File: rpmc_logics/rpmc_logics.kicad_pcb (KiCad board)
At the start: 2 copper layers, 56 x 60.5 mm, 9 parts, among them J1 Raspberry_Pi_2_3, J2 Conn_02x20_Odd_Even, U1 74HC373, U2 74HC373, U3 74LS139, U4 74LS139, U5 74LS139, U6 74HC04, U7 TXB0108PWR

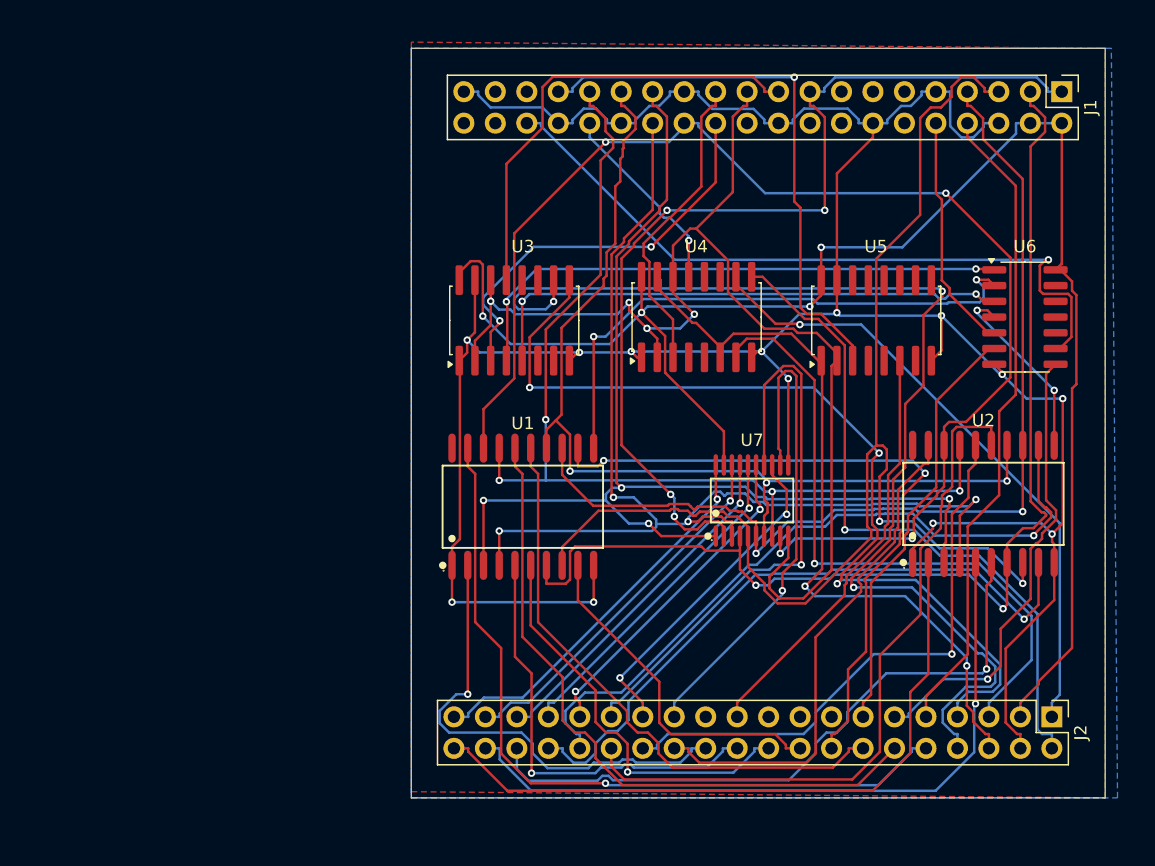
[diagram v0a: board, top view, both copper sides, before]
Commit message: libraries/PCM1808_EVB.kicad_mod libraries/footprint/PCM1808_EVB.kicad_mod libraries/footprint/msx-cartridge/libraries/packages3d/SOIC-20_L13.0-W7.6-P1.27-LS10.3-BL.step libraries/msx.pretty/Library.pretty/PCM1808_EVB.kicad_mod libraries/msx.pretty/PCM1808_EVB.kicad_mod libraries/msx_slot.kicad_sym libraries/footprint/msx-cartridge/libraries/packages3d/TSSOP-20_L6.5-W4.4-P0.65-LS6.4-BL.step -> libraries/packages3d/TSSOP-20_L6.5-W4.4-P0.65-LS6.4-BL.step rpmc_epm240/fp-info-cache rpmc_epm240/fp-lib-table rpmc_epm240/rpmc_epm240-backups/rpmc_epm240-2024-09-23_004329.zip rpmc_epm240/rpmc_epm240-backups/rpmc_epm240-2024-09-23_005415.zip rpmc_epm240/rpmc_epm240-backups/rpmc_epm240-2024-09-23_010603.zip rpmc_epm240/rpmc_epm240-backups/rpmc_epm240-2024-09-23_011813.zip rpmc_epm240/rpmc_epm240-backups/rpmc_epm240-2024-09-23_012814.zip rpmc_epm240/rpmc_epm240-backups/rpmc_epm240-2024-09-23_100545.zip rpmc_epm240/rpmc_epm240.kicad_pcb rpmc_epm240/rpmc_epm240.kicad_prl rpmc_epm240/rpmc_epm240.kicad_pro rpmc_epm240/rpmc_epm240.kicad_sch rpmc_logics/fp-info-cache rpmc_logics/fp-lib-table rpmc_logics/rpmc_logics-backups/rpmc_logics-2024-09-21_014511.zip rpmc_logics/rpmc_logics.kicad_pcb rpmc_logics/rpmc_logics.kicad_prl rpmc_logics/rpmc_logics.kicad_sch rpmc_logics/sym-lib-table
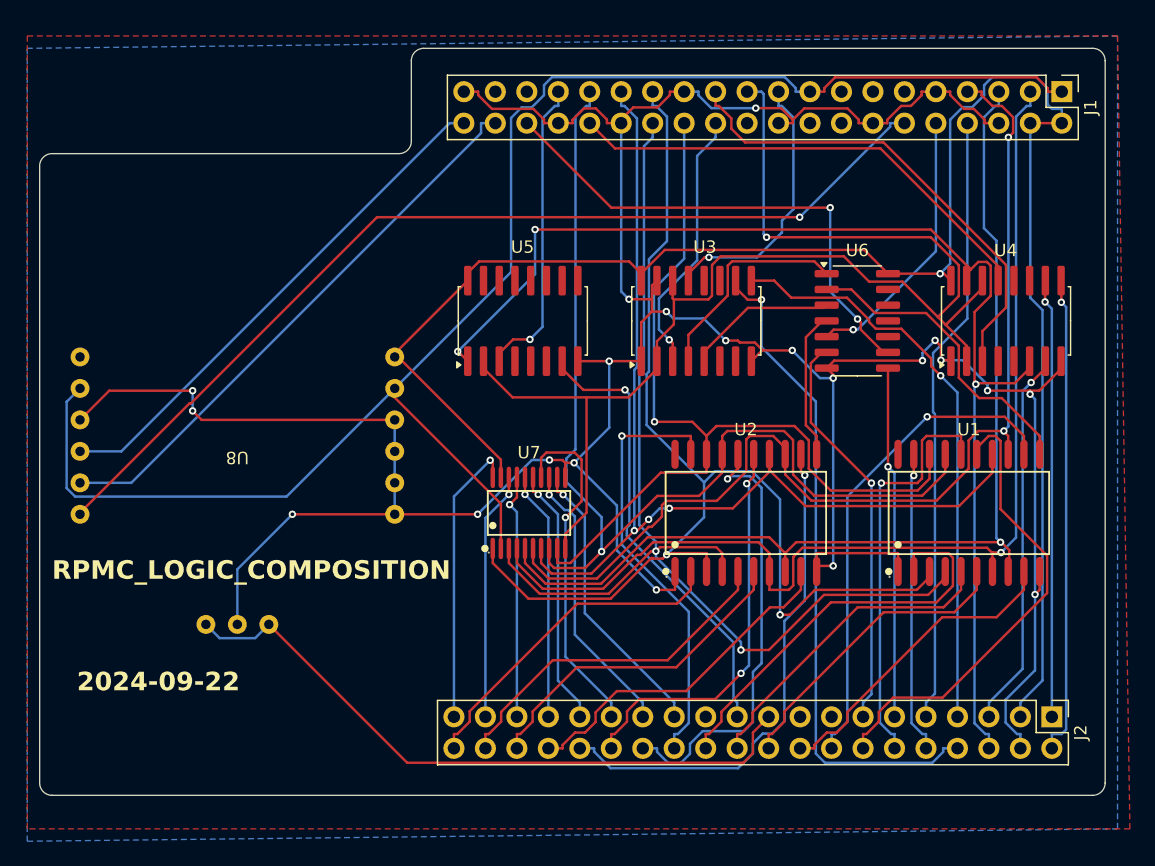
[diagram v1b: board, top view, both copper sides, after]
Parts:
- added U8: ~, footprint:PCM1808_EVB, F.Cu at (76.0, 60.3)
- moved U1 36.0 mm to (135.0, 66.5)
- moved U5 28.5 mm to (99.0, 51.0)
- moved U4 25.0 mm to (138.0, 51.0)
- moved U2 19.2 mm to (117.0, 66.5)
- moved U7 18.0 mm to (99.5, 66.5)
- moved U3 14.7 mm to (113.0, 51.0)
- moved U6 13.5 mm to (126.0, 51.0)
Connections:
- J1 pad 12: /G18 -> /BCK
- J1 pad 35: unconnected-(J1-GPIO19/MISO1-Pad35) -> /LRC
- J1 pad 38: unconnected-(J1-GPIO20/MOSI1-Pad38) -> /DIN
- J1 pad 40: unconnected-(J1-GPIO21/SCLK1-Pad40) -> /GCLK
- U5 pad 15: GND -> unconnected-(U5B-E-Pad15)
- U5 pad 6: /M1 -> unconnected-(U5A-O2-Pad6)
- U5 pad 7: unconnected-(U5A-O3-Pad7) -> /M1
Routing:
- net /BCK: track 0.00 -> 79.9 mm, vias 0 -> 1
- net GND: track 228.3 -> 282.9 mm, vias 13 -> 21
- net /SOUNDIN: track 0.00 -> 53.5 mm
- net +3V3: track 78.3 -> 129.3 mm, vias 4 -> 0
- net /DIN: track 0.00 -> 46.0 mm
- net /GCLK: track 0.00 -> 42.0 mm
- net /RD: track 92.1 -> 53.9 mm, vias 3 -> 1
- net /A15: track 62.5 -> 24.5 mm
- net /MREQ: track 60.7 -> 98.7 mm, vias 2 -> 3
- net /G7: track 106.3 -> 73.2 mm, vias 4 -> 1
- net /_ADDRH: track 43.7 -> 12.2 mm, vias 2 -> 0
- net /A1: track 58.0 -> 28.3 mm, vias 1 -> 0
- net /WR: track 75.6 -> 47.0 mm, vias 3 -> 1
- net /A0: track 55.7 -> 27.1 mm
- net /_ADDRL: track 45.4 -> 17.6 mm, vias 2 -> 0
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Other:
- board size 56 x 60.5 mm -> 86 x 60.3 mm
- board text added: "2024-09-22"
- board text added: "RPMC_LOGIC_COMPOSITION"

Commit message: rpmc_logics/fp-info-cache rpmc_logics/fp-lib-table rpmc_logics/rpmc_logics.kicad_pcb rpmc_logics/rpmc_logics.kicad_sch
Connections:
- U3 pad 13: /G10 -> /G9
- U3 pad 14: /G9 -> /G10
- U3 pad 2: /G9 -> /G8
- U3 pad 3: /G8 -> /G9
- U4 pad 13: /G12 -> /G9
- U4 pad 14: /G9 -> /G12
- U4 pad 2: /G9 -> /G11
- U4 pad 3: /G11 -> /G9
- U5 pad 2: /G9 -> /G13
- U5 pad 3: /G13 -> /G9
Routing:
- net /G3: track 84.5 -> 106.7 mm
- net /G9: track 107.1 -> 88.5 mm
- net /MREQ: track 98.7 -> 116.6 mm, vias 3 -> 2
- net +5V: track 143.1 -> 131.3 mm, vias 1 -> 0
- net +3V3: track 129.3 -> 118.7 mm, vias 0 -> 1
- net /G12: track 38.9 -> 48.9 mm, vias 0 -> 2
- net /A8: track 33.6 -> 24.7 mm
- net /WR: track 47.0 -> 54.9 mm, vias 1 -> 3
- net /D5: track 28.1 -> 21.9 mm
- net /A14: track 33.4 -> 27.6 mm
- net /G1: track 88.4 -> 82.8 mm, vias 2 -> 1
- net /A7: track 35.1 -> 29.5 mm
- net /G5: track 82.7 -> 88.2 mm, vias 3 -> 1
- net /A15: track 24.5 -> 28.0 mm
- net /G8: track 21.6 -> 24.9 mm
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
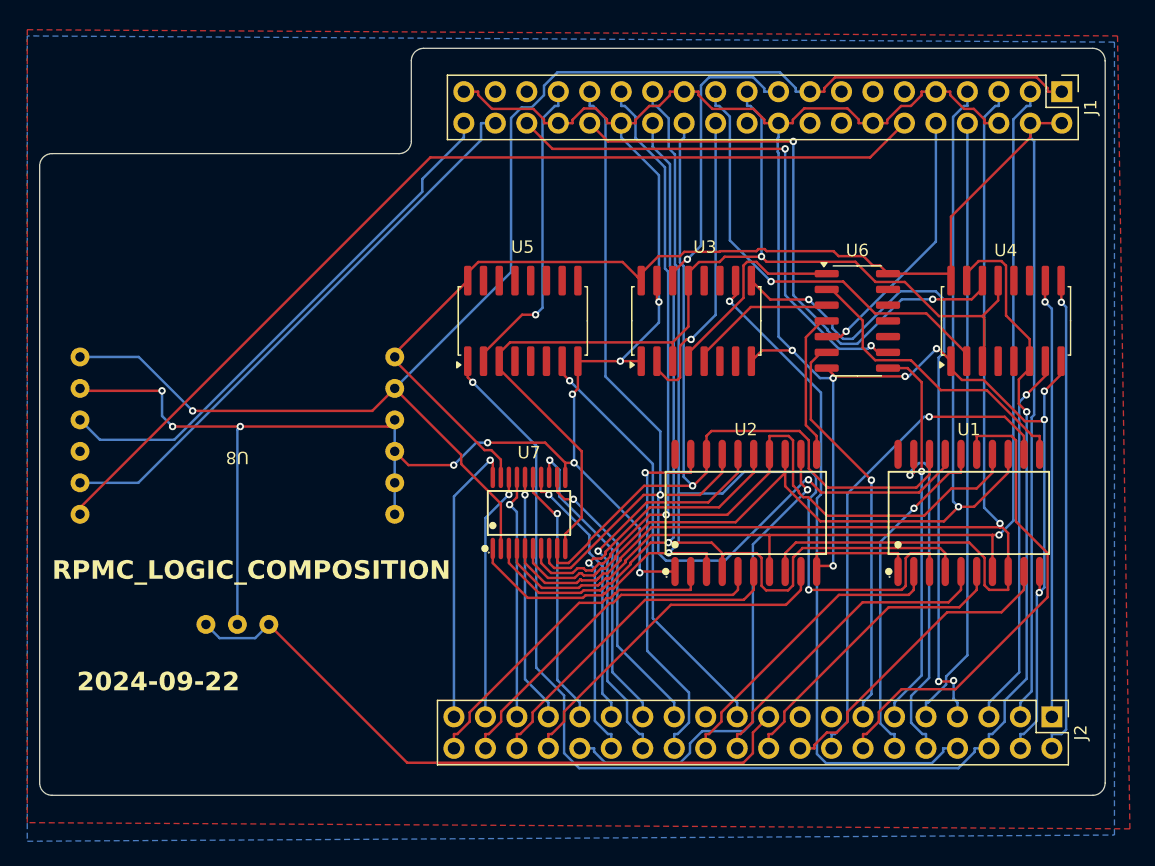
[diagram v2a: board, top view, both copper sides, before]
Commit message: rpmc_epm240/rpmc_epm240.kicad_prl rpmc_logics/rpmc_logics.kicad_pcb rpmc_logics/rpmc_logics.kicad_prl rpmc_logics/rpmc_logics.kicad_sch universal_msxcart/universal_msxcart.kicad_pcb
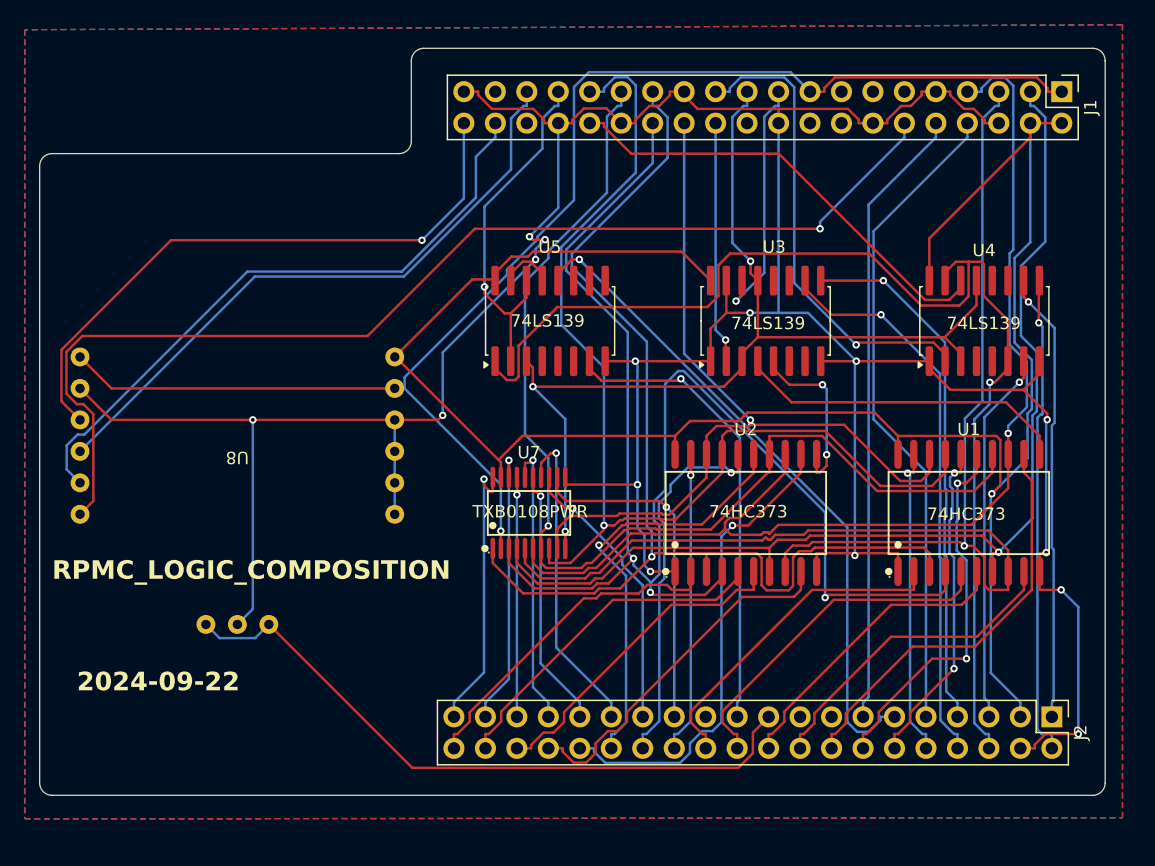
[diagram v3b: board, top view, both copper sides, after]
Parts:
- removed U6: 74HC04, Package_SO:SOIC-14_3.9x8.7mm_P1.27mm
- moved U3 5.60 mm to (118.6, 51.0)
- moved U5 2.20 mm to (101.2, 51.0)
- moved U4 1.75 mm to (136.2, 51.0)
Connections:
- net /WAIT renamed /G14
- J2 pad 13: /INT -> /G15
- U1 pad 20: unconnected-(U1-VCC-Pad20) -> +5V
- U2 pad 20: unconnected-(U2-VCC-Pad20) -> +5V
- U3 pad 4: /_ADDRL -> /ADDRL
- U3 pad 5: /_ADDRH -> /ADDRH
- U5 pad 12: unconnected-(U5B-O0-Pad12) -> /RESET
- U5 pad 13: unconnected-(U5B-A1-Pad13) -> GND
- U5 pad 14: unconnected-(U5B-A0-Pad14) -> /G13
- U5 pad 15: unconnected-(U5B-E-Pad15) -> GND
- U8 pad 12: (no net) -> /LRC
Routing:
- net /LRC: track 0.00 -> 51.2 mm
- net /G16: track 43.9 -> 0.00 mm, vias 2 -> 0
- net /G1: track 82.8 -> 116.9 mm, vias 1 -> 3
- net +5V: track 131.3 -> 164.3 mm, vias 0 -> 1
- net /INT: track 32.5 -> 0.00 mm, vias 1 -> 0
- net /G15: track 21.5 -> 50.4 mm, vias 1 -> 0
- net /RESET: track 31.1 -> 53.9 mm
- net /MREQ: track 116.6 -> 97.3 mm, vias 2 -> 1
- net /_ADDRL: track 16.8 -> 0.00 mm
- net /_ADDRH: track 12.1 -> 0.00 mm
- net /WR: track 54.9 -> 42.9 mm, vias 3 -> 1
- net /G12: track 48.9 -> 37.0 mm, vias 2 -> 0
- net /BCK: track 79.9 -> 91.0 mm, vias 0 -> 1
- net GND: track 282.2 -> 293.1 mm, vias 18 -> 15
- net /A13: track 39.6 -> 30.4 mm, vias 0 -> 2
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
